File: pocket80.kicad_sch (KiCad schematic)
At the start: 3 parts, among them U3 PIO-PLCC-44, U4 SIO3-PLCC-44, U5 CTC-PLCC-44

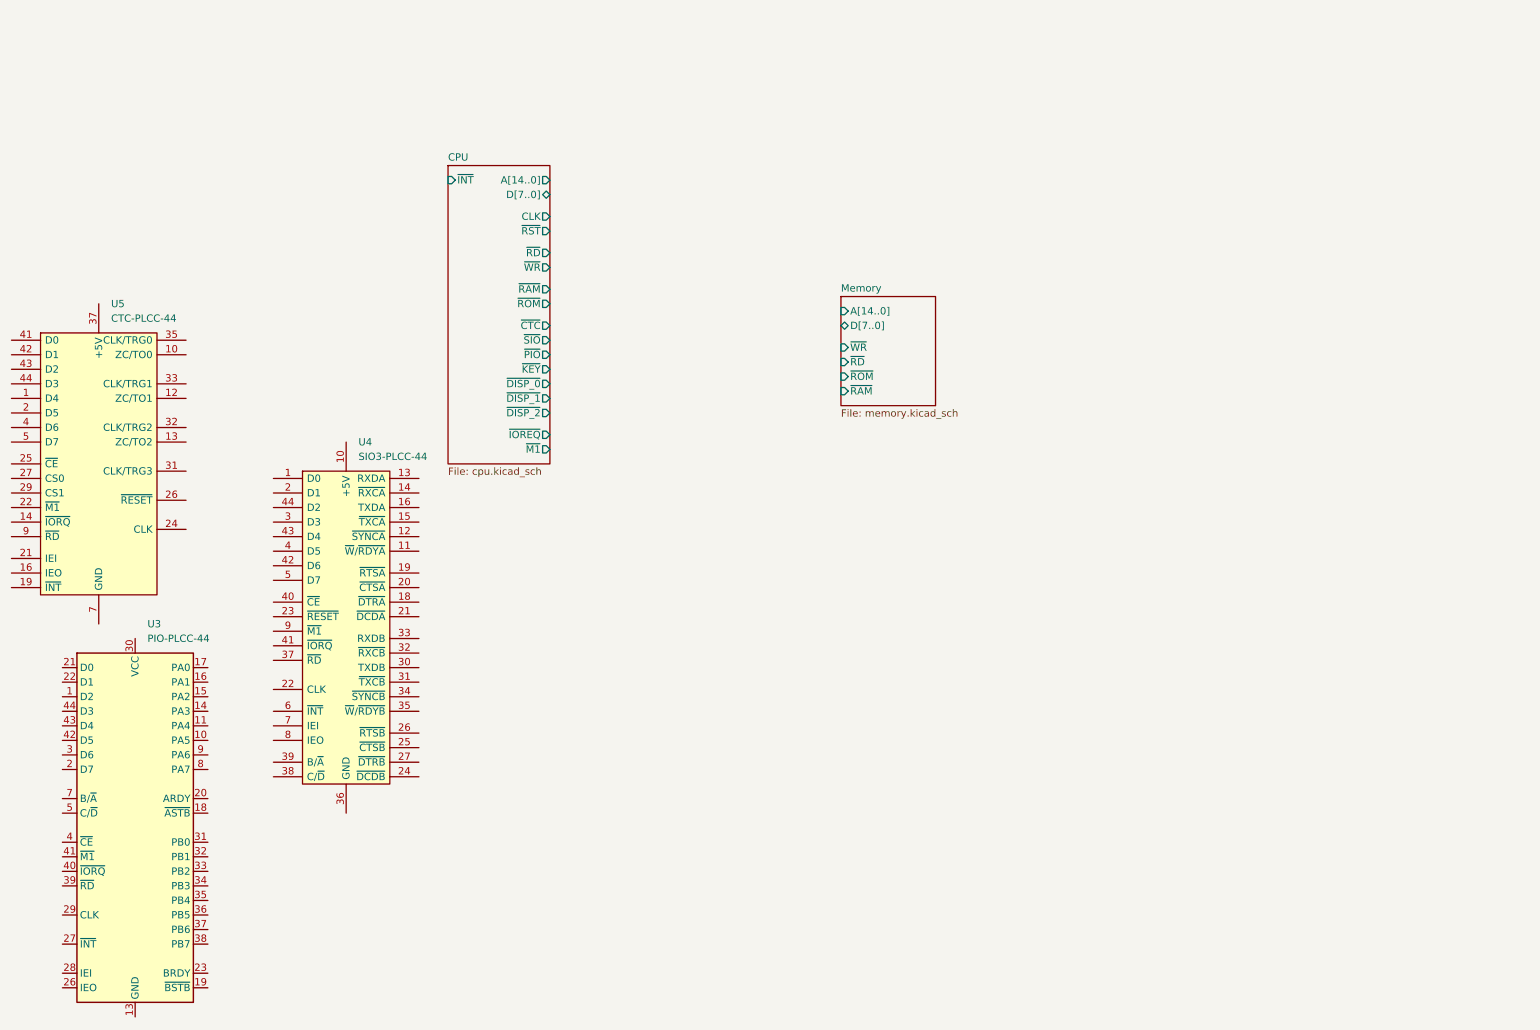
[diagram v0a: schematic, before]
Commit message: HW: Initial placement of I/O chips
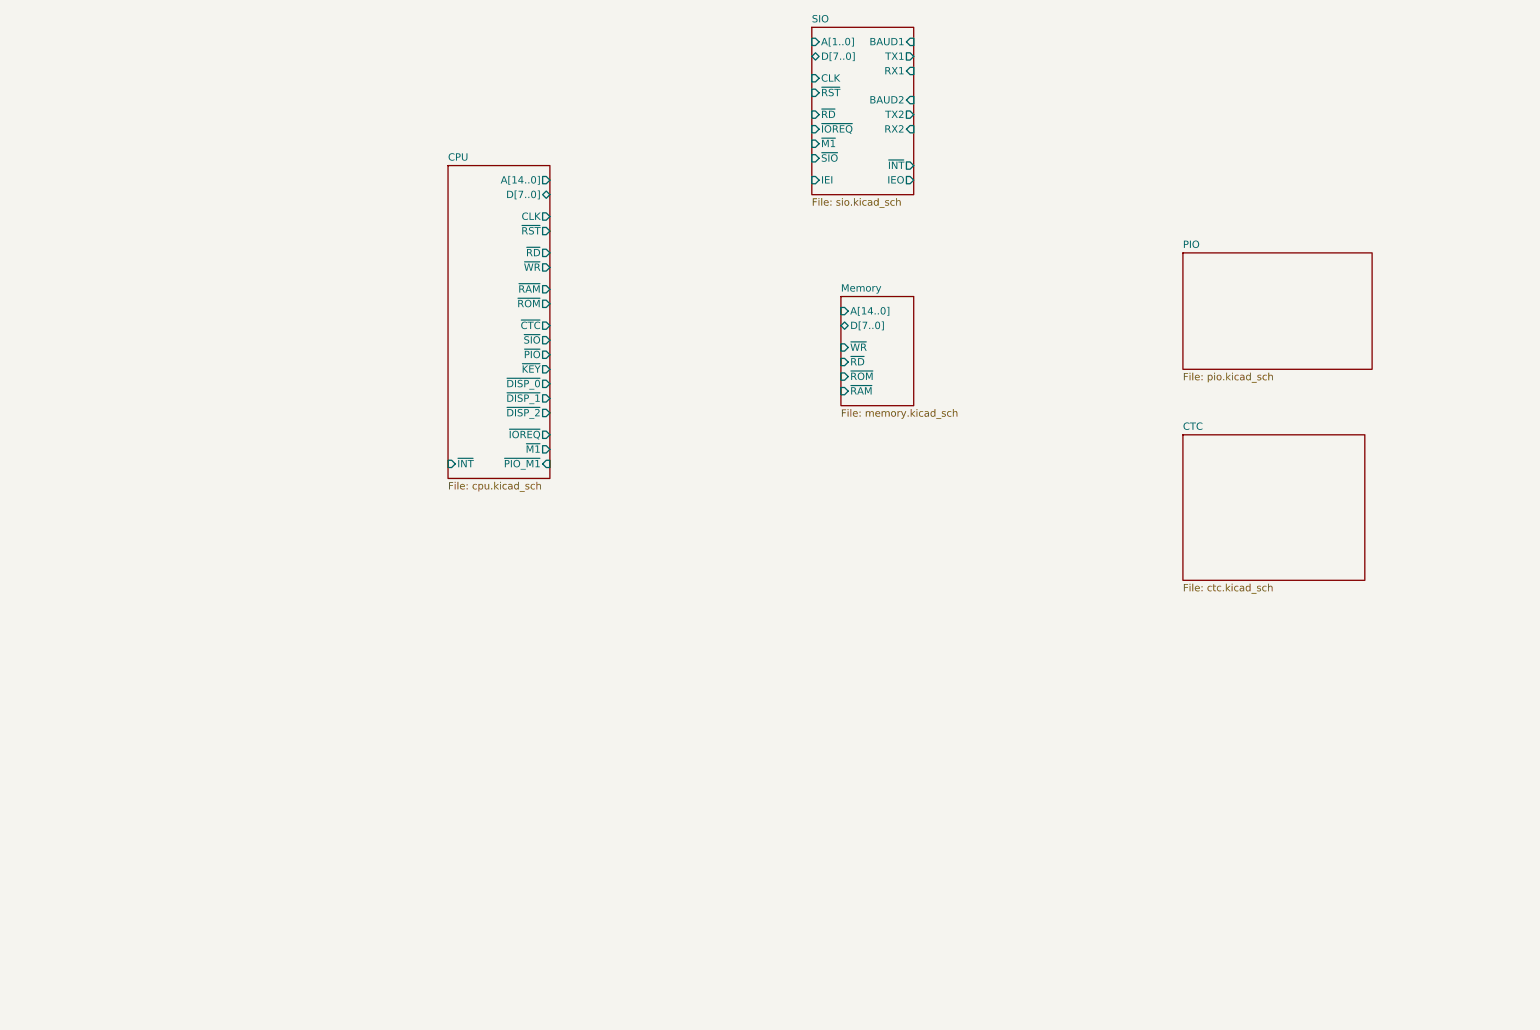
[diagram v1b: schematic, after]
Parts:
- removed U3: PIO-PLCC-44, Package_LCC:PLCC-44, symbol Zilog_Z80_Peripherals:PIO-PLCC-44
- removed U4: SIO3-PLCC-44, Package_LCC:PLCC-44, symbol Zilog_Z80_Peripherals:SIO3-PLCC-44
- removed U5: CTC-PLCC-44, Package_LCC:PLCC-44, symbol Zilog_Z80_Peripherals:CTC-PLCC-44
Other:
- added sheet CTC (ctc.kicad_sch)
- added sheet PIO (pio.kicad_sch)
- added sheet SIO (sio.kicad_sch)
- sheet CPU ports: added ~{PIO_M1}; removed none

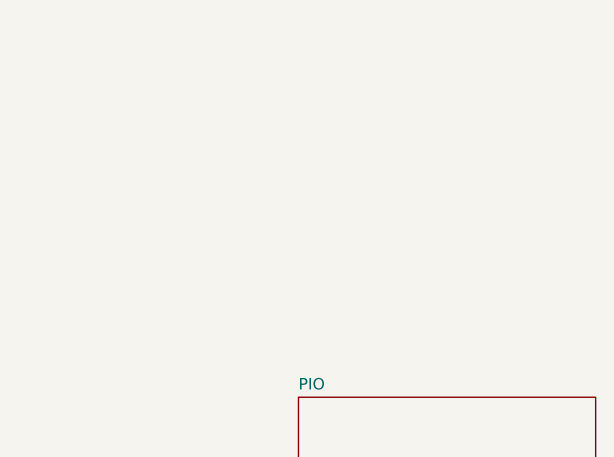
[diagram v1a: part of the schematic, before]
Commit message: HW: Add keyboard
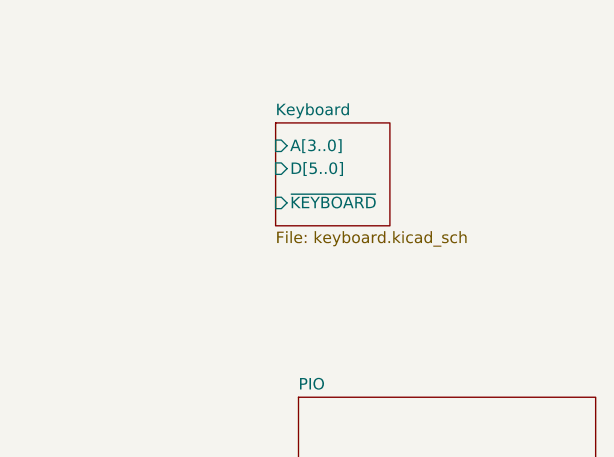
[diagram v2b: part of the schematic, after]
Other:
- added sheet Keyboard (keyboard.kicad_sch)
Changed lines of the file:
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@@
+		)
+	)
+	(sheet
+		(at 219.71 40.64)
+		(size 12.7 11.43)
+		(exclude_from_sim no)
+		(in_bom yes)
+		(on_board yes)
+		(dnp no)
+		(fields_autoplaced yes)
+		(stroke
+			(width 0.1524)
+			(type solid)
+		)
+		(fill
+			(color 0 0 0 0.0000)
+		)
+		(property "Sheetname" "Keyboard"
+			(at 219.71 39.9284 0)
+			(effects
+				(font
+					(size 1.27 1.27)
+				)
+				(justify left bottom)
+			)
+		)
+		(property "Sheetfile" "keyboard.kicad_sch"
+			(at 219.71 52.6546 0)
+			(effects
+				(font
+					(size 1.27 1.27)
+				)
+				(justify left top)
+			)
+		)
+		(pin "A[3..0]" input
+			(at 219.71 43.18 180)
+			(effects
+				(font
+					(size 1.27 1.27)
+				)
+				(justify left)
+			)
+		)
+		(pin "D[5..0]" input
+			(at 219.71 45.72 180)
+			(effects
+				(font
+					(size 1.27 1.27)
+				)
+				(justify left)
+			)
+		)
+		(pin "~{KEYBOARD}" input
+			(at 219.71 49.53 180)
+			(effects
+				(font
+					(size 1.27 1.27)
+				)
+				(justify left)
+			)
+		)
+		(instances
+			(project "pocket80"
+				(path "/328c075d-c706-4d2d-bd37-a88a0c604482"
+					(page "7")
+				)
+			)
 		)
 	)

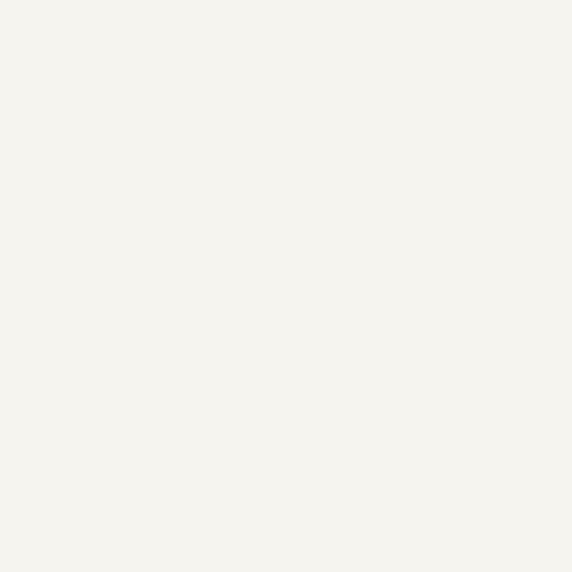
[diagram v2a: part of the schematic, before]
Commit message: HW: Add USB-C and battery charger
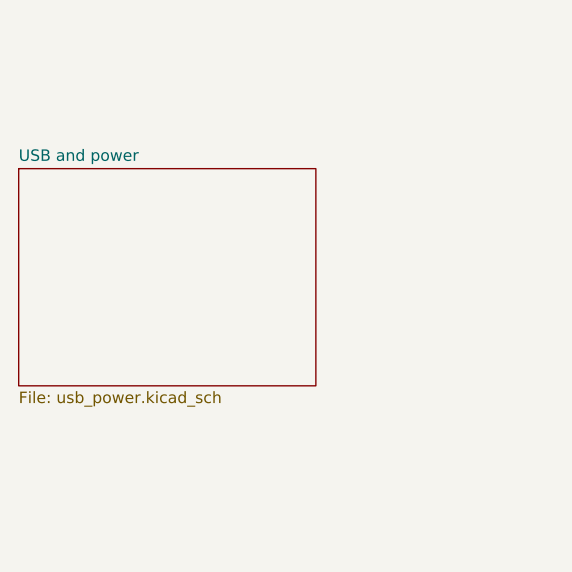
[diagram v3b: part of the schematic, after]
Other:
- added sheet USB and power (usb_power.kicad_sch)
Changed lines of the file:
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@@
+	)
+	(sheet
+		(at 25.4 45.72)
+		(size 33.02 24.13)
+		(exclude_from_sim no)
+		(in_bom yes)
+		(on_board yes)
+		(dnp no)
+		(fields_autoplaced yes)
+		(stroke
+			(width 0.1524)
+			(type solid)
+		)
+		(fill
+			(color 0 0 0 0.0000)
+		)
+		(property "Sheetname" "USB and power"
+			(at 25.4 45.0084 0)
+			(effects
+				(font
+					(size 1.27 1.27)
+				)
+				(justify left bottom)
+			)
+		)
+		(property "Sheetfile" "usb_power.kicad_sch"
+			(at 25.4 70.4346 0)
+			(effects
+				(font
+					(size 1.27 1.27)
+				)
+				(justify left top)
+			)
+		)
+		(instances
+			(project "pocket80"
+				(path "/328c075d-c706-4d2d-bd37-a88a0c604482"
+					(page "8")
+				)
+			)
+		)
 	)
 	(sheet

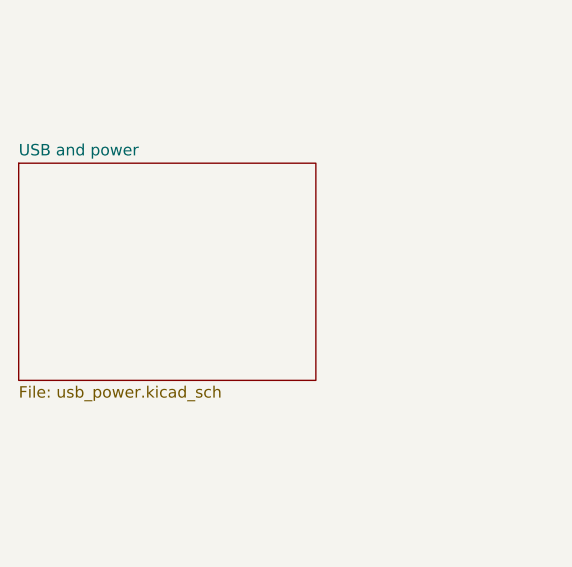
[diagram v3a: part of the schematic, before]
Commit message: HW: Update schematic info frames
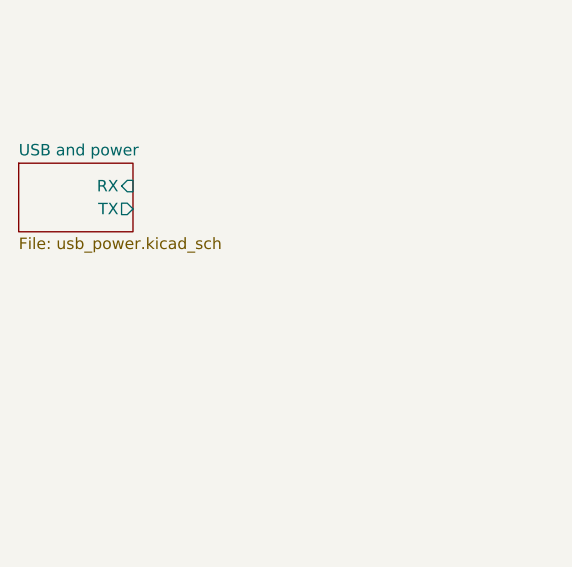
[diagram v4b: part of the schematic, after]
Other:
- sheet USB and power ports: added RX, TX; removed none
- company: (none) -> A.K.
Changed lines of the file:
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@@
 	(generator_version "9.0")
 	(paper "A4")
+	(title_block
+		(date "2025-10-14")
+		(rev "A")
+		(company "A.K.")
+	)
 	(sheet
 		(at 162.56 78.74)
@@
 	(sheet
 		(at 25.4 45.72)
-		(size 33.02 24.13)
+		(size 12.7 7.62)
 		(exclude_from_sim no)
 		(in_bom yes)
@@
 		)
 		(property "Sheetfile" "usb_power.kicad_sch"
-			(at 25.4 70.4346 0)
+			(at 25.4 53.9246 0)
 			(effects
 				(font
@@
 			)
 		)
+		(pin "RX" input
+			(at 38.1 48.26 0)
+			(effects
+				(font
+					(size 1.27 1.27)
+				)
+				(justify right)
+			)
+		)
+		(pin "TX" output
+			(at 38.1 50.8 0)
+			(effects
+				(font
+					(size 1.27 1.27)
+				)
+				(justify right)
+			)
+		)

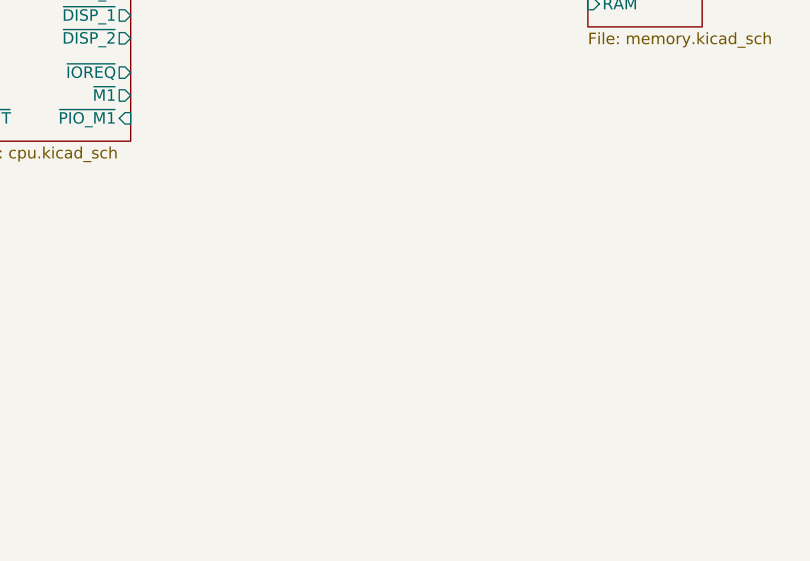
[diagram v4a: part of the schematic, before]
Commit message: HW: Add display, start PCB placement
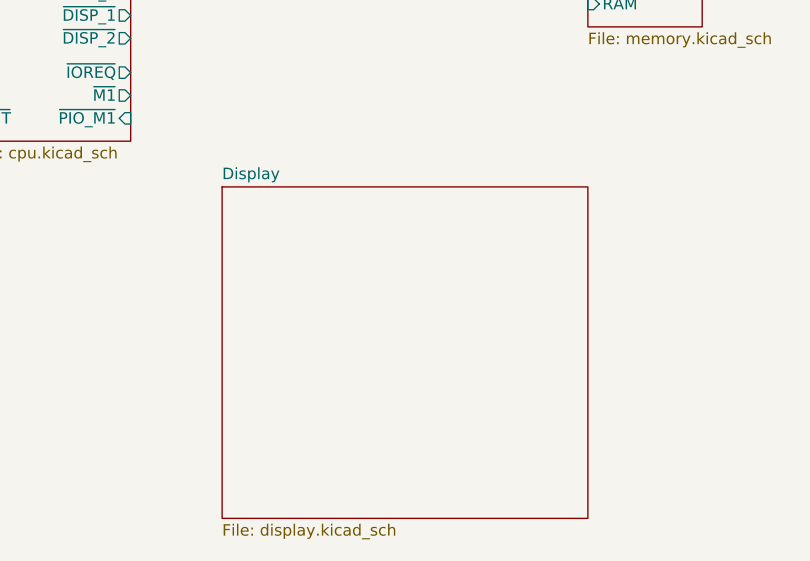
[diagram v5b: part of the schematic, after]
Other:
- added sheet Display (display.kicad_sch)
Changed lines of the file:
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@@
+	)
+	(sheet
+		(at 121.92 115.57)
+		(size 40.64 36.83)
+		(exclude_from_sim no)
+		(in_bom yes)
+		(on_board yes)
+		(dnp no)
+		(fields_autoplaced yes)
+		(stroke
+			(width 0.1524)
+			(type solid)
+		)
+		(fill
+			(color 0 0 0 0.0000)
+		)
+		(property "Sheetname" "Display"
+			(at 121.92 114.8584 0)
+			(effects
+				(font
+					(size 1.27 1.27)
+				)
+				(justify left bottom)
+			)
+		)
+		(property "Sheetfile" "display.kicad_sch"
+			(at 121.92 152.9846 0)
+			(effects
+				(font
+					(size 1.27 1.27)
+				)
+				(justify left top)
+			)
+		)
+		(instances
+			(project "pocket80"
+				(path "/328c075d-c706-4d2d-bd37-a88a0c604482"
+					(page "9")
+				)
+			)
+		)
 	)
 	(sheet
